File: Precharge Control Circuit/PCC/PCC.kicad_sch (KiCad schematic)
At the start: 128 parts, among them J1 Conn_01x04_Socket, J10 AMP BYP, J11 AMP BYP, J2 874271202, J3 462070206, J4 Conn_02x14_Counter_Clockwise, J5 IMD, J6 Thermistor Expansion, J7 RTM, J8 BMS, J9 EnergyMeter, K1 Relay_SPDT, K2 PCN-112D3MHZ_000, Q1 IRLZ44N, Q2 IRLZ44N, U1 SN65HVD230, U2 4N35, U3 4N35, U7 TLV2372IP, U8 LM1117T-5.0

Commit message: Lucas Out
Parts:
- added H1, H2, H3, H4: MountingHole_Pad, MountingHole:MountingHole_3.2mm_M3_DIN965_Pad_TopBottom, symbol Mechanical:MountingHole_Pad
- U7: footprint P8 -> footprints:P8
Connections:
- no-connect marks 19 -> 23

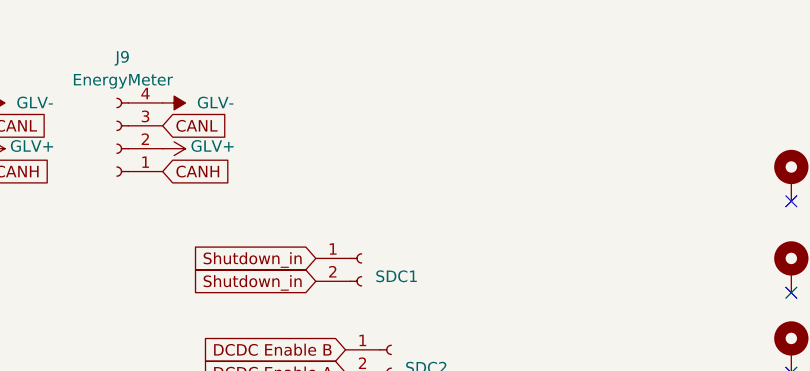
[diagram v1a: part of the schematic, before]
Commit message: PCC rev added port
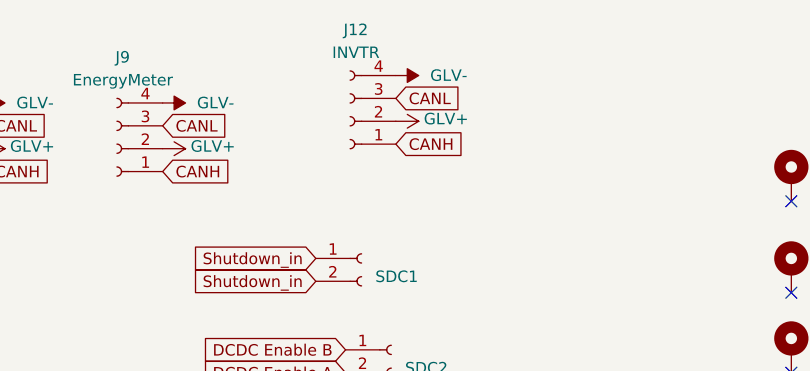
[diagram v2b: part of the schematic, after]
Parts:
- added J12: INVTR, Connector_Molex:Molex_Mini-Fit_Jr_5566-04A2_2x02_P4.20mm_Vertical, symbol Connector:Conn_01x04_Socket
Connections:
- net CANH: now also J12.1 (Pin_1)
- net CANL: now also J12.3 (Pin_3)
- net GLV+: now also J12.2 (Pin_2)
- net GLV-: now also J12.4 (Pin_4)

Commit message: updates I think
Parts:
- U7: MPN LM393P -> TLV2372IP
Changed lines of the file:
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@@
 			)
 		)
-		(property "MPN" "LM393P"
+		(property "MPN" "TLV2372IP"
 			(at 435.61 173.99 90)
 			(effects

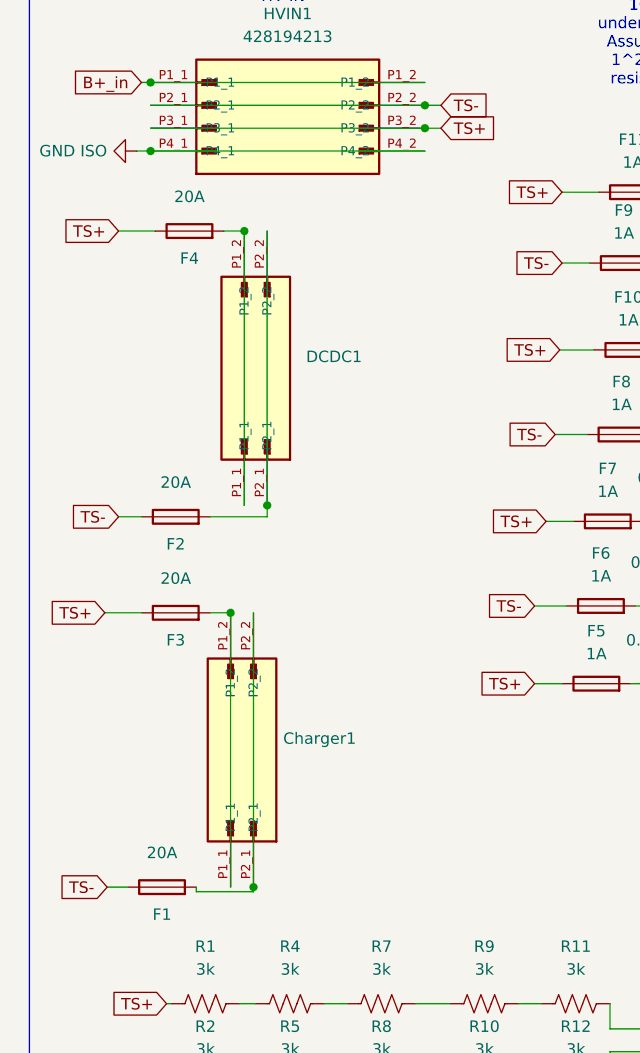
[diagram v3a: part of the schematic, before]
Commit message: fuse holders added
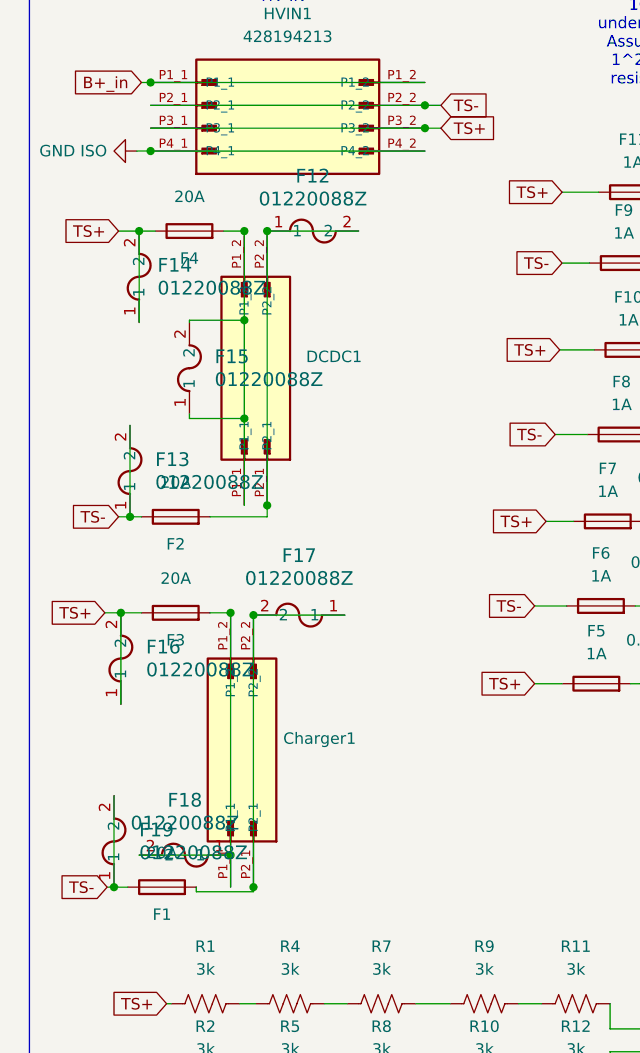
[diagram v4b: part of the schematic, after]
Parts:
- added F12, F13, F14, F15, F16, F17, F18, F19: 01220088Z, footprints:FuseHolder, symbol FuseHolder:01220088Z
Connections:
- net TS+: now also F14.1, F14.2, F16.1, F16.2
- net TS-: now also F13.1, F13.2, F19.1, F19.2
- net at Charger1.P2_1, Charger1.P2_2, F1.2: now also F17.1, F17.2
- net at DCDC1.P1_1, DCDC1.P1_2, F4.2: now also F15.1, F15.2
- net at DCDC1.P2_1, DCDC1.P2_2, F2.2: now also F12.1, F12.2
- net at Charger1.P1_1, Charger1.P1_2, F3.2: now also F18.1, F18.2

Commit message: PCCv2 started
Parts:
- removed Charger1, DCDC1: 428192213, footprints:MOLEX_428192213, symbol 428192213:428192213
- removed D2: 1N4007, Diode_THT:D_DO-41_SOD81_P10.16mm_Horizontal, symbol Diode:1N4007
- removed F12, F13, F14, F15, F16, F17, F18, F19: 01220088Z, footprints:FuseHolder, symbol FuseHolder:01220088Z
- removed HVIN1: 428194213, footprints:MOLEX_428194213, symbol 428194213:428194213
- removed J7: RTM, Connector_Molex:Molex_Mini-Fit_Jr_5566-04A2_2x02_P4.20mm_Vertical, symbol Connector:Conn_01x04_Socket
- removed K2: PCN-112D3MHZ_000, footprints:RELAY_PCN-105D3MHZ_000_TEC, symbol relay:PCN-112D3MHZ_000
- removed SDC2: Conn_01x02_Socket, Connector_Molex:Molex_Mini-Fit_Jr_5566-02A2_2x01_P4.20mm_Vertical, symbol Connector:Conn_01x02_Socket
- added H5, H6, H7, H8: MountingHole_Pad, MountingHole:MountingHole_3.2mm_M3_DIN965_Pad_TopBottom, symbol Mechanical:MountingHole_Pad
- added HS1, HS2: Heatsink_Pad, footprints:heatsink, symbol Mechanical:Heatsink_Pad
- added J13: 462070206, footprints:6pMinifitJR, symbol 6pMiniftJR:462070206
- added R78, R79, R80, R81: 0.43R 1/2W, Resistor_SMD:R_0805_2012Metric_Pad1.20x1.40mm_HandSolder, symbol Device:R_US
- F1, F2, F3, F4: value 20A -> 1A; footprint footprints:ЗAВ 33x7mm fuse(axial lead) -> footprints:5x20fuseblock; MFG Littelfuse Inc. -> Schurter; MPN 0505020.MXEP -> 0031.8222
- K1: footprint Relay_THT:Precharge_Discharge_Relay -> footprints:Precharge_Discharge_Relay_Rincon
- R3, R6: value 500 -> 2.7k; footprint footprints:Ohmite HS100 500R F -> Package_TO_SOT_THT:TO-220-2_Vertical; MFG (none) -> Vishay Sfernice; MPN (none) -> RTO020F27000JTE3
- renumbered F5 to F13, F6 to F14, F7 to F15, F8 to F16, F9 to F17, F10 to F18, F11 to F19, J12 to J10, J10 to J11, J11 to J12
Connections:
- net B+_in: now also J13.4
- net GND ISO: now also J13.3
- net TS+: now also F1.1, R80.2; no longer F3.1, F4.1, R1.1, R3.1
- net TS-: now also R81.2; no longer F1.1, K1.12, R2.1
- net TSMP+: now also J2.3; no longer J2.6
- net TSMP-: now also J2.2; no longer J2.12
- net Vin_Accu: now also R3.2; no longer R6.2
- net at F1.2: now also R78.1
- net TS+ unfused: now reaches R6.1
- net TS+ unfused: now also F3.1, R1.1, J13.1; no longer R3.2
- net at F4.2: now also R81.1
- net at F2.2: now also R79.1
- net at F3.2: now also R80.1
- net FusedTS + (expansion): now reaches J2.11
- net FusedTS + (expansion): now also R15.2
- net FusedTS+1 renamed FusedTS + (indicator)
- net FusedTS + (indicator): now also J2.6; no longer J2.2
- net FusedTS+2 renamed FusedTS + (IMD)
- net FusedTS + (IMD): now also J2.12; no longer J2.3
- net FusedTS+3 renamed FusedTS - (IMD)
- net FusedTS - (IMD): now also R16.2; no longer R15.2
- net FusedTS+4 renamed FusedTS + RTML
- net FusedTS + RTML: no longer J2.5
- net FusedTS-1: no longer names the net of J2.8
- net FusedTS-1: no longer R17.2
- net FusedTS-2: no longer names the net of J2.9
- net FusedTS-2: no longer R16.2
- net FusedTS-3: no longer names the net of J2.10
- net FusedTS-3: no longer R14.2
- net IL renamed FusedTS - (expansion)
- net FusedTS - (expansion): now also R14.2; no longer J2.1
- new net: R3.1, R6.2
- new net FusedTS - (indicator): J2.1, R17.2
- new net FusedTS - RTML: R79.2
- new net FusedTS+ (EM): J2.5, R78.2
- new net TS- unfused: F4.1, J13.6, K1.12, R2.1
- no-connect marks 23 -> 25
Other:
- added sheet RTM (RTM.kicad_sch)
- moved on the sheet: F13, R13

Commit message: PCC finalized
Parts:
- removed F13, F14, F15, F16, F17, F18, F2: 1A, footprints:5x20fuseblock, symbol Device:Fuse
- removed H5, H6, H7, H8: MountingHole_Pad, MountingHole:MountingHole_3.2mm_M3_DIN965_Pad_TopBottom, symbol Mechanical:MountingHole_Pad
- removed R10, R11, R12, R4, R5, R7, R8, R9: 3k, Resistor_SMD:R_2512_6332Metric, symbol Device:R_US
- removed R13, R14, R15, R16, R17, R18, R19, R78, R79, R80: 0.43R 1/2W, Resistor_SMD:R_0805_2012Metric_Pad1.20x1.40mm_HandSolder, symbol Device:R_US
- added F20, F21, F22, F23, F24, F25, F26: 1A, footprints:5x20fuseblock, symbol Device:Fuse
- added HS3, HS4: Heatsink_Pad, footprints:smolsink, symbol Mechanical:Heatsink_Pad
- added R82: 0.3r, Resistor_SMD:R_2512_6332Metric_Pad1.40x3.35mm_HandSolder, symbol Device:R_US
- F19: fuse inside (none) -> 0ADKC1000-BE
- F3: value 1A -> 1.25; fuse inside (none) -> 0ADKC1250-BE
- F4: value 1A -> 1.25; fuse inside (none) -> 0ADKC1250-BE , Bel Fuse Inc.
- J2: footprint footprints:12pRminifit -> footprints:12pSTminifit
- R1, R2: value 3k -> R_US; footprint Resistor_SMD:R_2512_6332Metric -> footprints:TO-220-2_Vertical-SMD; MFG Stackpole Electronics Inc -> Bourns Inc.; MPN RMCF2512JT3K00 -> PWR220T-35-1502J
- R81: value 0.43R 1/2W -> 0.3r; footprint Resistor_SMD:R_0805_2012Metric_Pad1.20x1.40mm_HandSolder -> Resistor_SMD:R_2512_6332Metric_Pad1.40x3.35mm_HandSolder; MFG Panasonic Electronic Components -> CSRN2512FKR300TR-ND; MPN ERJ-6DQFR43V -> CSRN2512FKR300
- U4, U5, U6: value ~ -> (none)
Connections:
- net FusedTS + (IMD): now also F21.2
- net FusedTS + (expansion): now also F23.2
- net FusedTS + (indicator): now also F19.2
- net FusedTS + RTML: now also F25.2
- net FusedTS - (IMD): now also F22.2
- net FusedTS - (expansion): now also F24.2
- net FusedTS - (indicator): now also F20.2
- net FusedTS - RTML: now also F26.2
- net FusedTS+ (EM): now also F1.2
- net GND ISO: now also J13.6; no longer J13.3
- net TS+: now also F21.1, F23.1, F25.1, R82.2
- net TS+ unfused: now also R1.2; no longer R1.1
- net TS-: now also F20.1, F22.1, F24.1, F26.1
- net TS- unfused: now also J13.3, R2.2; no longer J13.6, R2.1
- net TSMP+: now also R1.1
- net TSMP-: now also R2.1
- net at F3.2: now also R82.1
- no-connect marks 25 -> 27
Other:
- note added: "1.25A fuse has cold ohms of 134mohm. series resistor guarantees total reistance is >434mohm. s/c current is 420/0.434 = 968A which is less than 1kA fusing current at fusing current, series resistor dissapates 1.25^2*0.3 = 0.46875 W 0.47<<2W resistor rating"
- note added: "both TSMP resistors dissapate 420^2/30000 = 5.88W thats 2.94 W/resistor the heatsinks are rated for 16.3C/W (natural) temp rise is 16.3*2.94 = 47.9 C"
- note added: "each resistor dissapates 210v^2/2700r = 16.3W heatsink is 3.7 C/W heat rise 60.43 C rise"
- note removed: "1000 A fuse interrupt. under short 420/0.43=976.7A Assuming 1A fusing current 1^2*0.43 = 0.43W <1/2W resistors survive operating at fuse current"
- note removed: "Resistors are 1W rated. at 100s, 4.2v/cell = 420v rule states across TSMP 10 resistors in series 42v/resistor, 3k ohm 42^2/3000 = 0.588 W /resistor <<1W"

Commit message: PCC was rolled back rerolled it
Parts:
- K1: footprint footprints:Precharge_Discharge_Relay_Rincon -> footprints:RH3_Mount
- R1, R2: MFG Bourns Inc. -> Caddock Electronics Inc.; MPN PWR220T-35-1502J -> MP925-15.0K-1%
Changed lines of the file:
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@@
 			)
 		)
-		(property "Footprint" "footprints:Precharge_Discharge_Relay_Rincon"
+		(property "Footprint" "footprints:RH3_Mount"
 			(at 77.47 259.08 0)
 			(hide yes)
@@
 			)
 		)
-		(property "MPN" "PWR220T-35-1502J "
+		(property "MPN" "MP925-15.0K-1% "
 			(at 34.29 193.04 90)
 			(hide yes)
@@
 			)
 		)
-		(property "MFG" "Bourns Inc."
+		(property "MFG" "Caddock Electronics Inc."
 			(at 34.29 193.04 90)
 			(hide yes)
@@
 			)
 		)
-		(property "MPN" "PWR220T-35-1502J "
+		(property "MPN" "MP925-15.0K-1%  "
 			(at 34.29 185.42 90)
 			(hide yes)
@@
 			)
 		)
-		(property "MFG" "Bourns Inc."
+		(property "MFG" "Caddock Electronics Inc."
 			(at 34.29 185.42 90)
 			(hide yes)
